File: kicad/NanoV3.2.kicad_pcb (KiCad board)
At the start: 2 copper layers, 43.2 x 17.8 mm, 23 parts, among them IC2 LM1117IMPX-5.0, IC3 ATMEGA328P-AU, P1 TTL, P2 OUT, P3 INPUT, Q1 s9014, Y1 16MHz

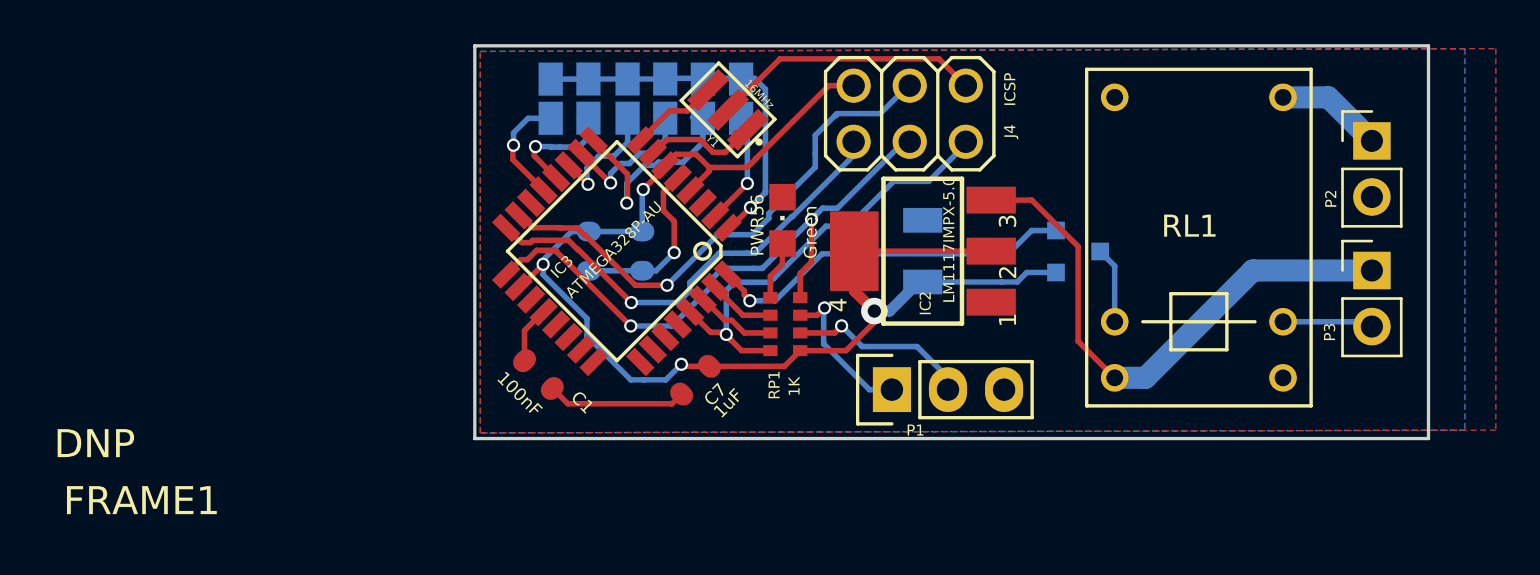
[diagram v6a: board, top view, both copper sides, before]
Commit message: update of routing to move the 4.7uf under the CPU
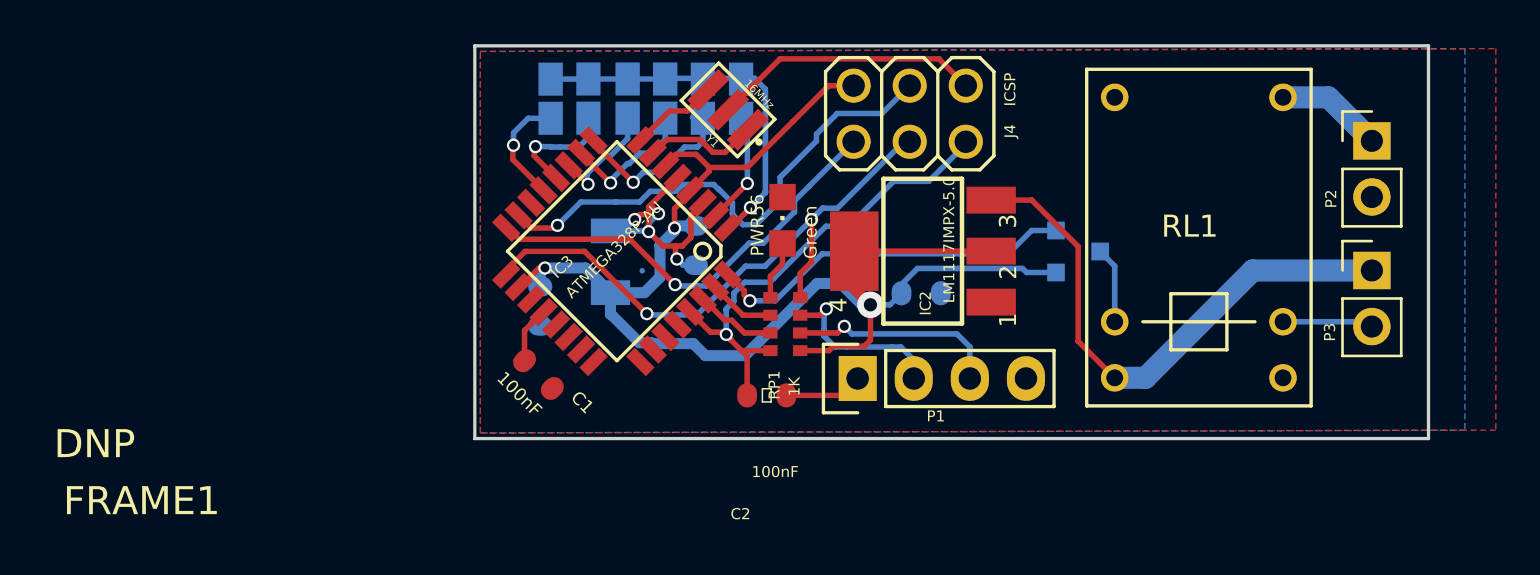
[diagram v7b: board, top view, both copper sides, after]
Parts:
- added C2: 100nF, C0603-ROUND, F.Cu at (140.1, 111.9)
- C7: moved to B.Cu
- P1: footprint Pin_Headers:Pin_Header_Straight_1x03 -> Pin_Headers:Pin_Header_Straight_1x04
- moved C5 14.1 mm to (133.1, 107.3)
- moved C7 10.9 mm to (147.1, 107.3), turned to 0 degrees
- moved C8 3.33 mm to (129.9, 107.9)
- moved C3 2.44 mm to (136.9, 105.2)
- moved P1 1.63 mm to (144.2, 111.2)
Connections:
- P1 pad 1: /TX -> Net-(C2-Pad2)
- P1 pad 2: Net-(P1-Pad2) -> /TX
- P1 pad 3: COM -> /RX
- RP1 pad 6: Net-(P1-Pad2) -> /RX
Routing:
- net /RX: track 0.00 -> 9.71 mm, vias 0 -> 1
- net Net-(P1-Pad2): track 8.42 -> 0.00 mm, vias 1 -> 0
- net +5V: track 61.8 -> 65.8 mm, vias 4 -> 3
- net Net-(C2-Pad2): track 0.00 -> 3.54 mm
- net /D5: track 10.2 -> 8.08 mm
- net /RESET: track 20.1 -> 22.0 mm
- net /D13/SCK: track 27.8 -> 27.2 mm
- net COM: track 31.9 -> 31.8 mm, vias 1 -> 4
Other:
- net class w0.5: clearance 0.4 -> 0.3

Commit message: minor update
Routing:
- net +5V: track 65.8 -> 70.6 mm
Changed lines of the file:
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@@
     (thickness 1.6)
     (drawings 89)
-    (tracks 364)
+    (tracks 381)
     (zones 0)
     (modules 24)
@@
     (tags CAPACITOR)
     (attr smd)
-    (fp_text reference C2 (at -1.18364 5.37464) (layer F.SilkS)
-      (effects (font (size 0.5 0.5) (thickness 0.1016)))
-    )
-    (fp_text value 100nF (at 0.381 3.46964) (layer F.SilkS)
-      (effects (font (size 0.5 0.5) (thickness 0.1016)))
+    (fp_text reference C2 (at -2.5146 -0.03556) (layer F.SilkS)
+      (effects (font (size 0.5 0.5) (thickness 0.05)))
+    )
+    (fp_text value 100nF (at -2.667 1.0668) (layer F.SilkS)
+      (effects (font (size 0.5 0.5) (thickness 0.05)))
     )
     (fp_line (start -0.8382 0.4699) (end -0.33782 0.4699) (layer Dwgs.User) (width 0.06604))
@@
   )
   (gr_line (start 147.7645 100.7872) (end 147.92075 100.748137) (layer Eco1.User) (width 0.15))
-  (segment (start 134.49046 106.299) (end 134.493 106.29646) (width 0.25) (layer Bottom) (net 0))
   (segment (start 136.00176 105.17632) (end 136.00176 105.70464) (width 0.25) (layer Top) (net 1))
   (segment (start 136.33958 106.04246) (end 136.91616 106.04246) (width 0.25) (layer Bottom) (net 1))
@@
   (segment (start 163.50488 108.60532) (end 167.3098 108.60532) (width 0.25) (layer Bottom) (net 1))
   (segment (start 167.3098 108.60532) (end 167.52824 108.82376) (width 0.25) (layer Bottom) (net 1))
+  (segment (start 137.24128 104.59212) (end 136.91616 104.267) (width 0.25) (layer Bottom) (net 2))
+  (segment (start 135.77316 104.10952) (end 136.75868 104.10952) (width 0.25) (layer Bottom) (net 2))
+  (segment (start 136.75868 104.10952) (end 136.91616 104.267) (width 0.25) (layer Bottom) (net 2))
+  (segment (start 136.017 104.8004) (end 136.38276 104.8004) (width 0.25) (layer Bottom) (net 2))
+  (segment (start 136.38276 104.8004) (end 136.91616 104.267) (width 0.25) (layer Bottom) (net 2))
+  (segment (start 135.48868 105.06456) (end 135.48868 104.96042) (width 0.25) (layer Bottom) (net 2))
+  (segment (start 135.48868 104.96042) (end 135.48868 104.394) (width 0.25) (layer Bottom) (net 2))
+  (segment (start 135.48868 104.394) (end 135.71728 104.1654) (width 0.25) (layer Bottom) (net 2))
+  (segment (start 135.70712 104.8004) (end 136.017 104.8004) (width 0.25) (layer Bottom) (net 2))
+  (segment (start 136.017 104.8004) (end 136.5504 104.267) (width 0.25) (layer Bottom) (net 2))
+  (segment (start 136.5504 104.267) (end 136.91616 104.267) (width 0.25) (layer Bottom) (net 2))
+  (segment (start 135.70712 104.84612) (end 135.70712 104.8004) (width 0.25) (layer Bottom) (net 2))
+  (segment (start 135.70712 104.8004) (end 135.70712 104.37368) (width 0.25) (layer Bottom) (net 2))
+  (segment (start 135.70712 104.37368) (end 135.71728 104.36352) (width 0.25) (layer Bottom) (net 2))
+  (segment (start 135.71728 104.36352) (end 135.71728 104.1654) (width 0.25) (layer Bottom) (net 2))
+  (segment (start 135.95604 104.25684) (end 135.95604 104.36352) (width 0.25) (layer Bottom) (net 2))
+  (segment (start 135.71728 104.1654) (end 135.77316 104.10952) (width 0.25) (layer Bottom) (net 2))
+  (segment (start 135.77316 104.10952) (end 135.80872 104.10952) (width 0.25) (layer Bottom) (net 2))
+  (segment (start 135.80872 104.10952) (end 135.95604 104.25684) (width 0.25) (layer Bottom) (net 2))
+  (segment (start 134.02564 106.31932) (end 133.05536 107.2896) (width 0.5) (layer Bottom) (net 2))
+  (segment (start 134.23392 106.31932) (end 134.02564 106.31932) (width 0.5) (layer Bottom) (net 2))
+  (segment (start 135.70712 104.84612) (end 135.48868 105.06456) (width 0.5) (layer Bottom) (net 2))
+  (segment (start 135.48868 105.06456) (end 134.23392 106.31932) (width 0.5) (layer Bottom) (net 2))
+  (segment (start 129.87528 107.0102) (end 132.77596 107.0102) (width 0.5) (layer Bottom) (net 2))
+  (segment (start 132.77596 107.0102) (end 133.05536 107.2896) (width 0.5) (layer Bottom) (net 2))
   (segment (start 133.05536 108.27004) (end 133.08076 108.27004) (width 0.5) (layer Bottom) (net 2))
   (segment (start 134.89432 109.55528) (end 134.89432 109.59592) (width 0.5) (layer Bottom) (net 2))
@@
   (segment (start 137.35304 110.13948) (end 139.14628 110.13948) (width 0.5) (layer Bottom) (net 2))
   (segment (start 136.80948 109.59592) (end 137.35304 110.13948) (width 0.5) (layer Bottom) (net 2))
+  (segment (start 144.82572 107.83824) (end 144.43964 107.83824) (width 0.5) (layer Bottom) (net 2))
+  (segment (start 144.43964 107.83824) (end 143.47444 106.87304) (width 0.5) (layer Bottom) (net 2))
+  (segment (start 143.47444 106.87304) (end 142.41272 106.87304) (width 0.5) (layer Bottom) (net 2))
+  (segment (start 142.41272 106.87304) (end 139.14628 110.13948) (width 0.5) (layer Bottom) (net 2))
+  (segment (start 133.05536 108.27004) (end 133.05536 107.2896) (width 0.5) (layer Bottom) (net 2))
   (segment (start 148.76272 106.19232) (end 151.70904 106.19232) (width 0.25) (layer Bottom) (net 2))
   (segment (start 151.70904 106.19232) (end 151.89196 106.37524) (width 0.25) (layer Bottom) (net 2))
@@
   (segment (start 151.89196 106.37524) (end 153.22804 106.37524) (width 0.25) (layer Bottom) (net 2))
   (segment (start 146.95424 106.19232) (end 148.76272 106.19232) (width 0.25) (layer Bottom) (net 2))
-  (segment (start 144.82572 107.83824) (end 144.43964 107.83824) (width 0.5) (layer Bottom) (net 2))
-  (segment (start 144.43964 107.83824) (end 143.47444 106.87304) (width 0.5) (layer Bottom) (net 2))
-  (segment (start 143.47444 106.87304) (end 142.41272 106.87304) (width 0.5) (layer Bottom) (net 2))
-  (segment (start 142.41272 106.87304) (end 139.14628 110.13948) (width 0.5) (layer Bottom) (net 2))
-  (segment (start 133.05536 108.27004) (end 133.05536 107.2896) (width 0.5) (layer Bottom) (net 2))
-  (segment (start 133.05536 107.2896) (end 134.595878 107.2896) (width 0.5) (layer Bottom) (net 2))
-  (segment (start 134.595878 107.2896) (end 135.29564 106.589838) (width 0.5) (layer Bottom) (net 2))
-  (segment (start 135.29564 106.589838) (end 135.29564 105.14584) (width 0.5) (layer Bottom) (net 2))
-  (segment (start 135.29564 105.14584) (end 135.95604 104.48544) (width 0.5) (layer Bottom) (net 2))
-  (segment (start 135.95604 104.48544) (end 135.95604 104.36352) (width 0.5) (layer Bottom) (net 2))
-  (segment (start 130.08864 106.172) (end 131.93776 106.172) (width 0.5) (layer Bottom) (net 2))
-  (segment (start 131.93776 106.172) (end 133.05536 107.2896) (width 0.5) (layer Bottom) (net 2))
   (segment (start 144.82572 107.83824) (end 145.70964 107.83824) (width 0.25) (layer Bottom) (net 2))
   (segment (start 145.70964 107.83824) (end 146.23288 107.315) (width 0.25) (layer Bottom) (net 2))
@@
   (via (at 135.95604 104.36352) (size 0.6) (drill 0.4) (layers Top Bottom) (net 2))
   (segment (start 136.00684 104.31272) (end 136.00684 104.267) (width 0.25) (layer Bottom) (net 2))
+  (segment (start 135.95604 104.36352) (end 136.00684 104.31272) (width 0.25) (layer Bottom) (net 2))
   (segment (start 136.91616 104.267) (end 136.00684 104.267) (width 0.5) (layer Bottom) (net 2))
-  (segment (start 135.95604 104.36352) (end 136.00684 104.31272) (width 0.25) (layer Bottom) (net 2))
   (segment (start 128.90046 107.031113) (end 128.914567 107.031113) (width 0.25) (layer Top) (net 2))
   (segment (start 129.87528 107.0102) (end 129.87528 106.35996) (width 0.5) (layer Bottom) (net 2))
